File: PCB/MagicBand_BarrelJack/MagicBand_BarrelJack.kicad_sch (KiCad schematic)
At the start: 19 parts, among them J2 MFRC522_Module, J3 RF_TX_DFLIFE, J6 NeoPixel_LED_Strip, J8 PWR_IN_BarrelJack_BareLeads, J9 ISP_AVR_2x3, Q1 AO3401A_PMOS_G-S-D, U1 ATmega328P-P, U2 MCP1700-3302, Y1 16MHz

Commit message: Source Y1 crystal, resize load caps 22pF -> 27pF
Picked a real, verified part (Euroquartz HC49-4H, 16MHz, 18pF rated
load capacitance, THT, matches the board's existing footprint) to
close the placeholder flagged since the design plan was written.
Sized C1/C2 from that CL rating via the standard load-cap formula.
ERC unchanged (129, exact baseline) -- value-only edit.

Also found and flagged (not fixed) a real schematic/PCB footprint
mismatch on C2/C6 while cross-checking package sizes for sourcing --
looks like a swap, not two independent errors. Needs a placement call
before touching those pads.

Co-Authored-By: Claude Sonnet 5 <noreply@anthropic.com>
Claude-Session: https://claude.ai/code/session_01UiULxbNnG293uuE4csn9nG
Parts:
- C1, C2: value 22pF -> 27pF
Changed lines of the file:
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@@
 			(effects (font (size 1.27 1.27)))
 		)
-		(property "Value" "22pF"
+		(property "Value" "27pF"
 			(at 121.43 66.26 0)
 			(effects (font (size 1.27 1.27)))
@@
 			(effects (font (size 1.27 1.27)))
 		)
-		(property "Value" "22pF"
+		(property "Value" "27pF"
 			(at 149.05 66.26 0)
 			(effects (font (size 1.27 1.27)))

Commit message: Fix C2/C6 footprint mismatch: schematic to match PCB, no board changes
C2 was documented as 0603 but 0805 pads are what's actually on the
already-routed, PDR-approved board; C6 was the reverse. Rather than
touch fab-ready copper, re-pointed the schematic's Footprint property
on both to match physical reality. Confirmed via git diff that the
.kicad_pcb has zero changed lines. ERC unchanged (129, exact
baseline).

Co-Authored-By: Claude Sonnet 5 <noreply@anthropic.com>
Claude-Session: https://claude.ai/code/session_01UiULxbNnG293uuE4csn9nG
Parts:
- C2: footprint Capacitor_SMD:C_0603_1608Metric -> Capacitor_SMD:C_0805_2012Metric
- C6: footprint Capacitor_SMD:C_0805_2012Metric -> Capacitor_SMD:C_0603_1608Metric
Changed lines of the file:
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@@
 			(effects (font (size 1.27 1.27)))
 		)
-		(property "Footprint" "Capacitor_SMD:C_0603_1608Metric"
+		(property "Footprint" "Capacitor_SMD:C_0805_2012Metric"
 			(at 149.05 69.76 0)
 			(effects (font (size 1.27 1.27)) (hide yes))
@@
 			(effects (font (size 1.27 1.27)))
 		)
-		(property "Footprint" "Capacitor_SMD:C_0805_2012Metric"
+		(property "Footprint" "Capacitor_SMD:C_0603_1608Metric"
 			(at 280 150 0)
 			(effects (font (size 1.27 1.27)) (hide yes))

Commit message: Generate PCBA assembly BOM/CPL, DNP J8, fix C_AREF annotation
User wants everything fab-placeable sent to assembly, hand-work
minimized to what genuinely can't be (J8's bare pads, plug-in
modules). Verified first that no PCB copper changes were needed --
JLCPCB-class services support mixed SMT+THT in one order, so 18 of 19
refs qualify as-is.

Two real fixes, both documentation-level: J8 marked dnp=yes in both
schematic and PCB (it's bare pads by design, not a real part -- an
assembly order would otherwise try to place a generic header there).
C_AREF renamed to C8 -- was never properly annotated, which risked a
BOM/CPL reference mismatch in an actual assembly order, not just a
cosmetic warning.

Generated MagicBand_BarrelJack_BOM.csv and _CPL.csv, ready to upload
to a fab quote tool. Both verified via ERC/DRC diff against exact
baseline (129/7) -- caught and fixed a dropped-paren mistake in the
C8 rename before it reached any exported file.

Co-Authored-By: Claude Sonnet 5 <noreply@anthropic.com>
Claude-Session: https://claude.ai/code/session_01UiULxbNnG293uuE4csn9nG
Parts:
- J8: now not fitted
- renumbered C_AREF to C8
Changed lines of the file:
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@@
 		(on_board yes)
 		(dnp no)
-		(property "Reference" "C_AREF"
+		(property "Reference" "C8"
 			(at 110 124 0)
 			(effects (font (size 1.27 1.27)))
@@
 			(project "MagicBand_BarrelJack"
 				(path "/bcfef247-dfd6-4ae3-b42f-2bc22ccfcf8a"
-					(reference "C_AREF")
+					(reference "C8")
 					(unit 1)
 				)
@@
 		(in_bom yes)
 		(on_board yes)
-		(dnp no)
+		(dnp yes)
 		(property "Reference" "J8"
 			(at 250 124 0)

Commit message: Flip J2/J3 to hand-solder DNP, confirm Q1 JLCPCB part
During live JLCPCB BOM matching, decided J2 (MFRC522 socket) and J3
(RF TX header) should be hand-soldered rather than fab-placed, since
both take repeated mechanical stress (module insertion/removal, wire
tension) and solder-joint reliability matters more there than
one-shot assembly convenience. J6 and J9 stay fab-placed (keyed/
pre-built mating cables, no equivalent stress concern). Q1 confirmed
at JLCPCB: AO3401A, C15127, Basic tier, Alpha & Omega Semi.

Set dnp yes on J2/J3 in schematic + PCB (same mechanism as J8's
existing DNP flag), regenerated BOM.csv, re-derived CPL.csv (confirmed
byte-identical to before -- DNP lives in the BOM column only, per the
prior J8 CPL-completeness finding). ERC/DRC re-verified unchanged
(129/7).

Co-Authored-By: Claude Sonnet 5 <noreply@anthropic.com>
Claude-Session: https://claude.ai/code/session_01UiULxbNnG293uuE4csn9nG
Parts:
- J2, J3: now not fitted
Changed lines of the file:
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@@
 		(in_bom yes)
 		(on_board yes)
-		(dnp no)
+		(dnp yes)
 		(property "Reference" "J2"
 			(at 250 34 0)
@@
 		(in_bom yes)
 		(on_board yes)
-		(dnp no)
+		(dnp yes)
 		(property "Reference" "J3"
 			(at 290 34 0)

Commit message: J2 moved to fab-placed; live BOM verification caught MCU Qty=0 bug
Verified two successive live JLCPCB BOM exports at @user's request.
Export (3) had U1 (the ATmega328P MCU), C7, and R1/R2 all showing
Qty=0/Price=$0 despite a real part match -- confirmed genuine
exclusion (not a display artifact) by matching the row-price sum to
the export's own listed total. Would have shipped 5 boards with no
MCU populated. @user fixed it in JLCPCB's tool; export (4) re-verified
clean (price sum matches $17.38 exactly, all three now Qty>0).

J2 (MFRC522 socket) reversed from 2026-08-25's hand-solder decision
back to fab-placed -- the reliability reasoning was a preference, not
a technical blocker, and a plain 1x8 female 2.54mm socket is generic
(2.54MM 1X8P RED, JLCPCB C9900138233). Un-flagged dnp in both the
schematic and PCB, ERC/DRC re-verified unchanged (129/7, 0 unconnected)
before and after, BOM.csv regenerated. J3 intentionally left hand-solder.
U1 socket-vs-direct-chip also closed out: direct chip, per @user.

Co-Authored-By: Claude Sonnet 5 <noreply@anthropic.com>
Claude-Session: https://claude.ai/code/session_01UiULxbNnG293uuE4csn9nG
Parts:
- J2: now fitted
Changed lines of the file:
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@@
 		(in_bom yes)
 		(on_board yes)
-		(dnp yes)
+		(dnp no)
 		(property "Reference" "J2"
 			(at 250 34 0)

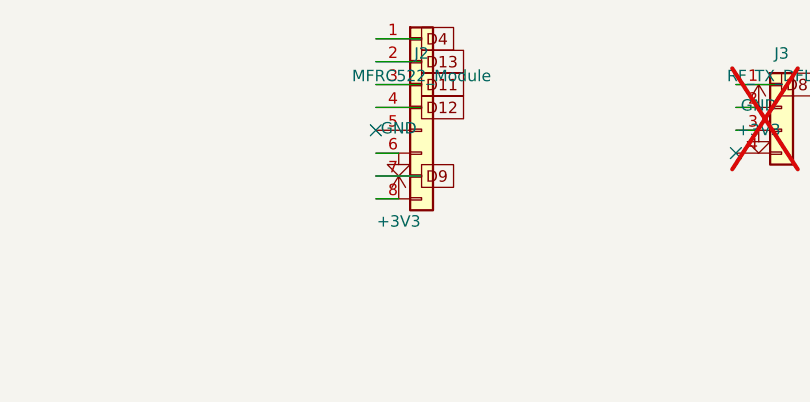
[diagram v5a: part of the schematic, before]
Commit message: J2 reverted to hand-solder; J2/J3 settled on direct-solder, no header needed
C9900138233 (J2's fab-placed socket from the prior commit) hit a part
shortage. Found a well-stocked fallback (BOOMELE 2.54-1x8P, C27438,
128k+ stock) but @user reconsidered the whole approach instead of
just swapping parts, and decided to hand-solder both J2 and J3.

Reverted J2's dnp flag back to yes in both the schematic and PCB
(exact reverse of the prior commit), re-verified ERC/DRC unchanged
(129/7, 0 unconnected -- third check on this same flag today, same
baseline every time), regenerated BOM.csv.

Clarified what "hand-solder" means here: no header/socket component
for either J2 or J3 at all -- each module's own pins solder directly
through the board's existing through-holes for a permanent, more
secure joint. Female-socket and male-header footprints share
identical hole geometry, so this needs no PCB change and, more
importantly, nothing left to buy for either connector's board-side
hardware. J9 stays a real connector (not direct-solder) since it's
repeatedly plugged/unplugged via the Nano ISP cable across multiple
boards, unlike J2/J3's permanent module attachments.

Co-Authored-By: Claude Sonnet 5 <noreply@anthropic.com>
Claude-Session: https://claude.ai/code/session_01UiULxbNnG293uuE4csn9nG
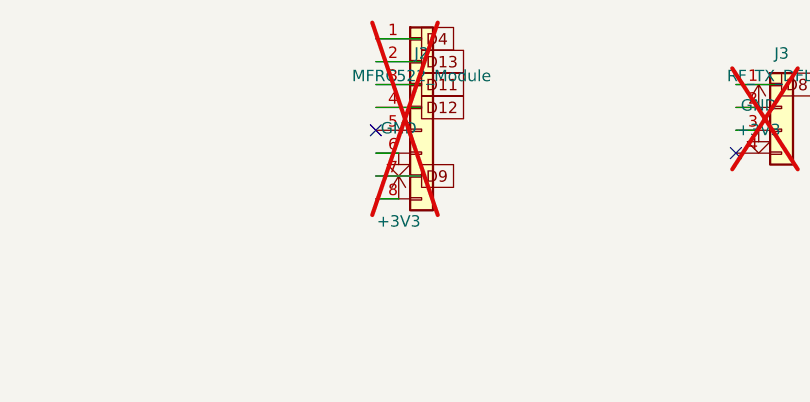
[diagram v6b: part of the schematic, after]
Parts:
- J2: now not fitted
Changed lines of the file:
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@@
 		(in_bom yes)
 		(on_board yes)
-		(dnp no)
+		(dnp yes)
 		(property "Reference" "J2"
 			(at 250 34 0)
